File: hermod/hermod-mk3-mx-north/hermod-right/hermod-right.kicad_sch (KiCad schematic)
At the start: 45 parts, among them J1 USB_C_Receptacle_USB2.0, J2 Conn_01x05, J3 USB_C_Receptacle_USB2.0, Q3 MMUN2133LT1G, U1 STM32G474CETx, U2 PRTR5V0U2X, U3 XC6206PxxxMR-Regulator_Linear, U4 CR2013-MI2120, U5 PRTR5V0U2X, U8 SN74AHCT1G125DBVR

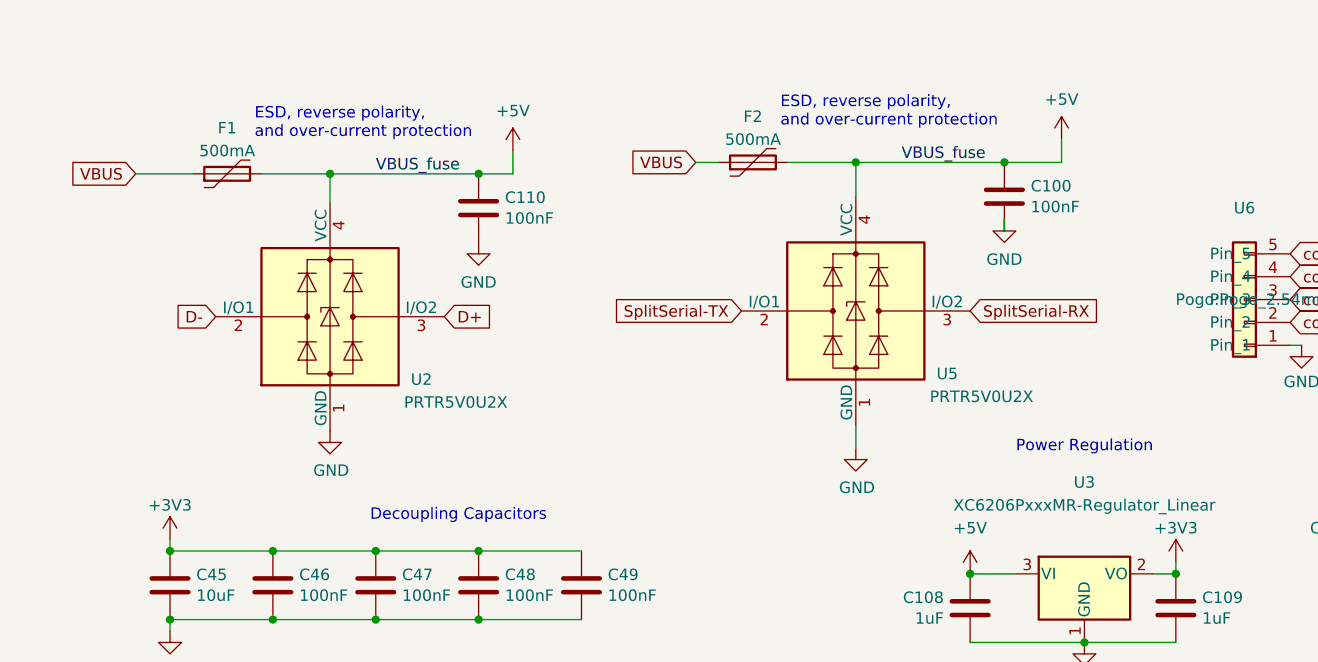
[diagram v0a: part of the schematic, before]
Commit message: Switched to SRV05-4
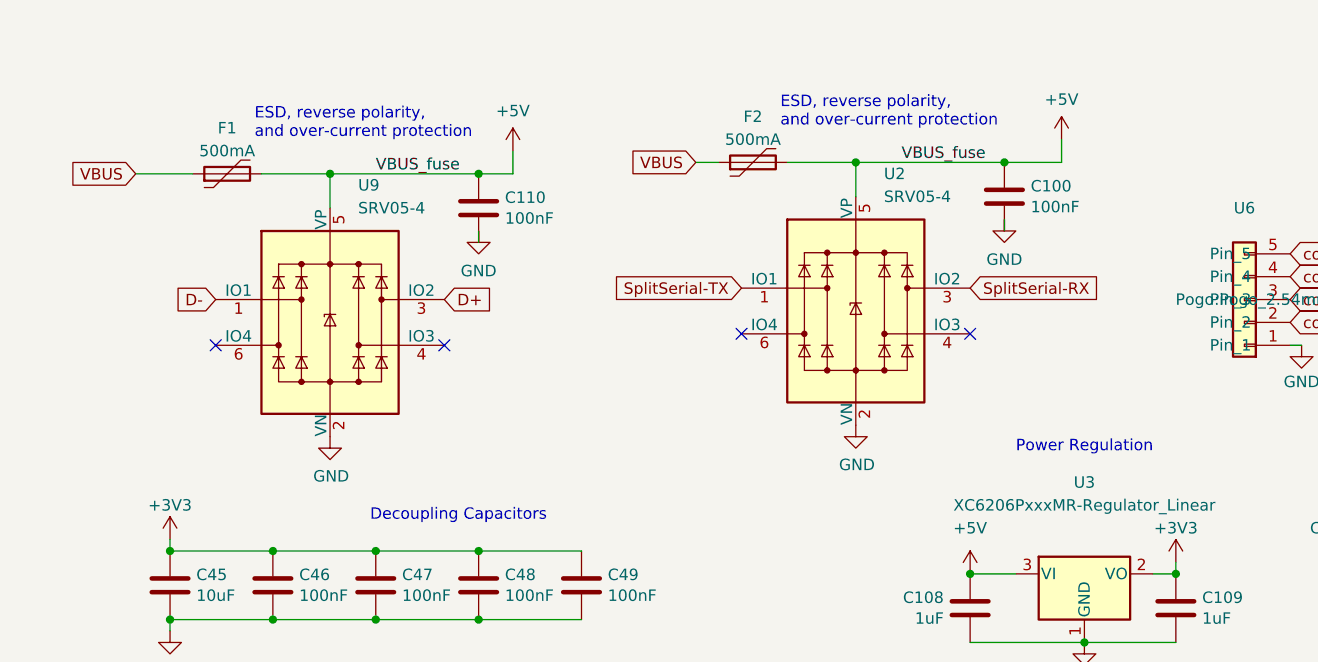
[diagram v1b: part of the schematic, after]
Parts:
- removed U2, U5: PRTR5V0U2X, Package_TO_SOT_SMD:SOT-143, symbol Power_Protection:PRTR5V0U2X
- added U2, U9: SRV05-4, PCM_marbastlib-various:SOT-23-6-routable, symbol PCM_marbastlib-various:SRV05-4
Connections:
- net +5V: now also U2.5 (VP), U9.5 (VP)
- net D+: now also U9.3 (IO2)
- net D-: now also U9.1 (IO1)
- net GND: now also U2.2 (VN), U9.2 (VN)
- net SplitSerial-RX: now also U2.3 (IO2)
- net SplitSerial-TX: now also U2.1 (IO1)
- no-connect marks 8 -> 12
